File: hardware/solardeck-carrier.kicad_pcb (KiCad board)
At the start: 6 copper layers, 222 x 160 mm, 24 parts, among them J1 DF40C-100DS-0.4V, J2 DF40C-100DS-0.4V, SW1 JS102011SAQN, U1 BQ25895RTWR, U10 W25Q128JVS, U11 DS3231MZ+, U14 TMUX1575PWR, U15 SN74LVC1G08DBVR, U16 VL805-Q6, U18 ST4SIM-200M, U2 TPS62840DLYR, U3 TPS61088RHLR, U4 TPS63020DSJR, U5 BQ25504RGTR, U8 RP2350B, U9 APS6404L-3SQR-SN

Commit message: hardware: fix TMUX1575 fake PN (PWR->YCJR) across all artifacts; make Rule 8 scan comp values
The repo shipped TMUX1575PWR -- a part number that does not exist (TI TMUX1575
is DSBGA-YCJ only, per HARDWARE_SPEC B2/ADR-004). The fake PN was in the netlist
comp value, PCB fp_text, display sheet, BOM/CPL CSVs and both Seeed BOM exports,
while audit Rule 8 only scanned net NAMES, so the ban was silently dead code.

- parse_netlist_comps() added; Rule 8 now audits both nets and comp values
  (negative-tested: a value-embedded TMUX1575PWR is caught).
- All artifacts normalized to TMUX1575YCJR; footprint marked DSBGA-16 with dims
  TBD from TI datasheet (no fabricated package size); display sheet comment
  corrected from the banned '8-Channel' framing to 4-channel x2 devices.

Co-Authored-By: DeepSeek V4-Flash 0731 <noreply@anthropic.com>
Harness: pi (openrouter/deepseek/deepseek-v4-flash-0731, session 01a15a7c)
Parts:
- U14: value TMUX1575PWR -> TMUX1575YCJR; footprint Package_SO:TSSOP-24_4.4x7.8mm_P0.65mm -> DSBGA-16 (dims per TI datasheet; see ADR-004)
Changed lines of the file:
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@@
   )
   ;; Display Section: TMUX1575 (U14), IT8951 40-pin FPC (J_EPDC), Palm Gate (U15)
-  (footprint "Package_SO:TSSOP-24_4.4x7.8mm_P0.65mm" (layer "F.Cu")
+  (footprint "DSBGA-16 (dims per TI datasheet; see ADR-004)" (layer "F.Cu")
     (at 85.0 25.0)
     (fp_text reference "U14" (at 0 -4.5) (layer "F.SilkS") (effects (font (size 1 1) (thickness 0.15))))
-    (fp_text value "TMUX1575PWR" (at 0 4.5) (layer "F.Fab") (effects (font (size 1 1) (thickness 0.15))))
+    (fp_text value "TMUX1575YCJR" (at 0 4.5) (layer "F.Fab") (effects (font (size 1 1) (thickness 0.15))))
     (pad "1" smd rect (at -2.8 -3.575) (size 1.4 0.4) (layers "F.Cu" "F.Paste" "F.Mask"))
   )

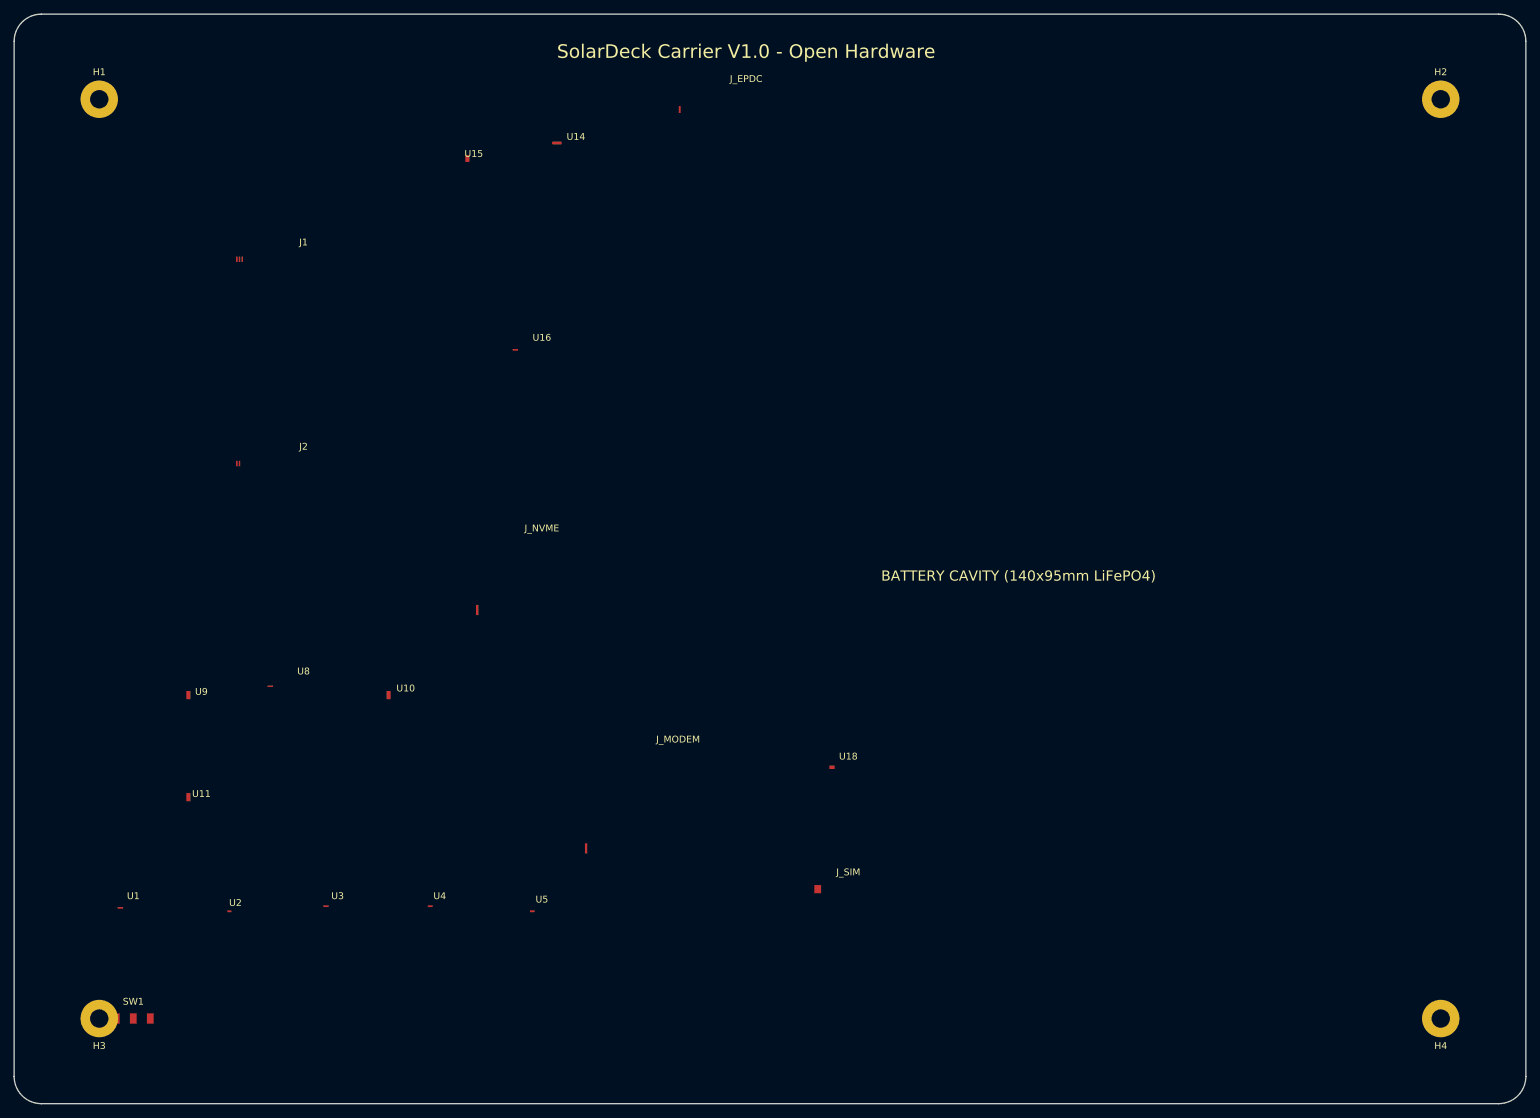
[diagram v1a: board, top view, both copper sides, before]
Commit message: schematic: capture 10 sensor/power/io BOM line items into the schematic layer (20/62 -> 30/62)
Adds U19-U28 with datasheet-anchored footprints and REAL sourced LCSC part
numbers (verified 2026-11-02): TPS22918DBVR, INA3221AIRGVR, BQ27441-G1A,
TPS2051BDBVR (power); BMA400, BMP390, TMP112AIDRLR (compute); TUSB320RWBR,
TXU0104PWR, MAX98357A (io).

Files moved in lockstep: .kicad_sch symbol blocks, netlist comps, BOM CSV rows,
CPL centroids (inside 222x160 board), kicad_pcb fp_text reference labels
(reference-grade single pads per U5/U14 convention; full pad maps and routing
remain the stated 'unrouted PCB' phase).

scripts/capture_schematic_parts.py is the generator + assert (Phase 11 contract:
netlist == BOM == CPL == 30 designators). spec_values schematic_coverage_baseline
20 -> 30; prose in README/BOM/HANDOFF normalized; STATUS.md regenerated.

Co-Authored-By: DeepSeek V4-Flash 0731 <noreply@anthropic.com>
Harness: pi (openrouter/deepseek/deepseek-v4-flash-0731, session 01a15a7c)
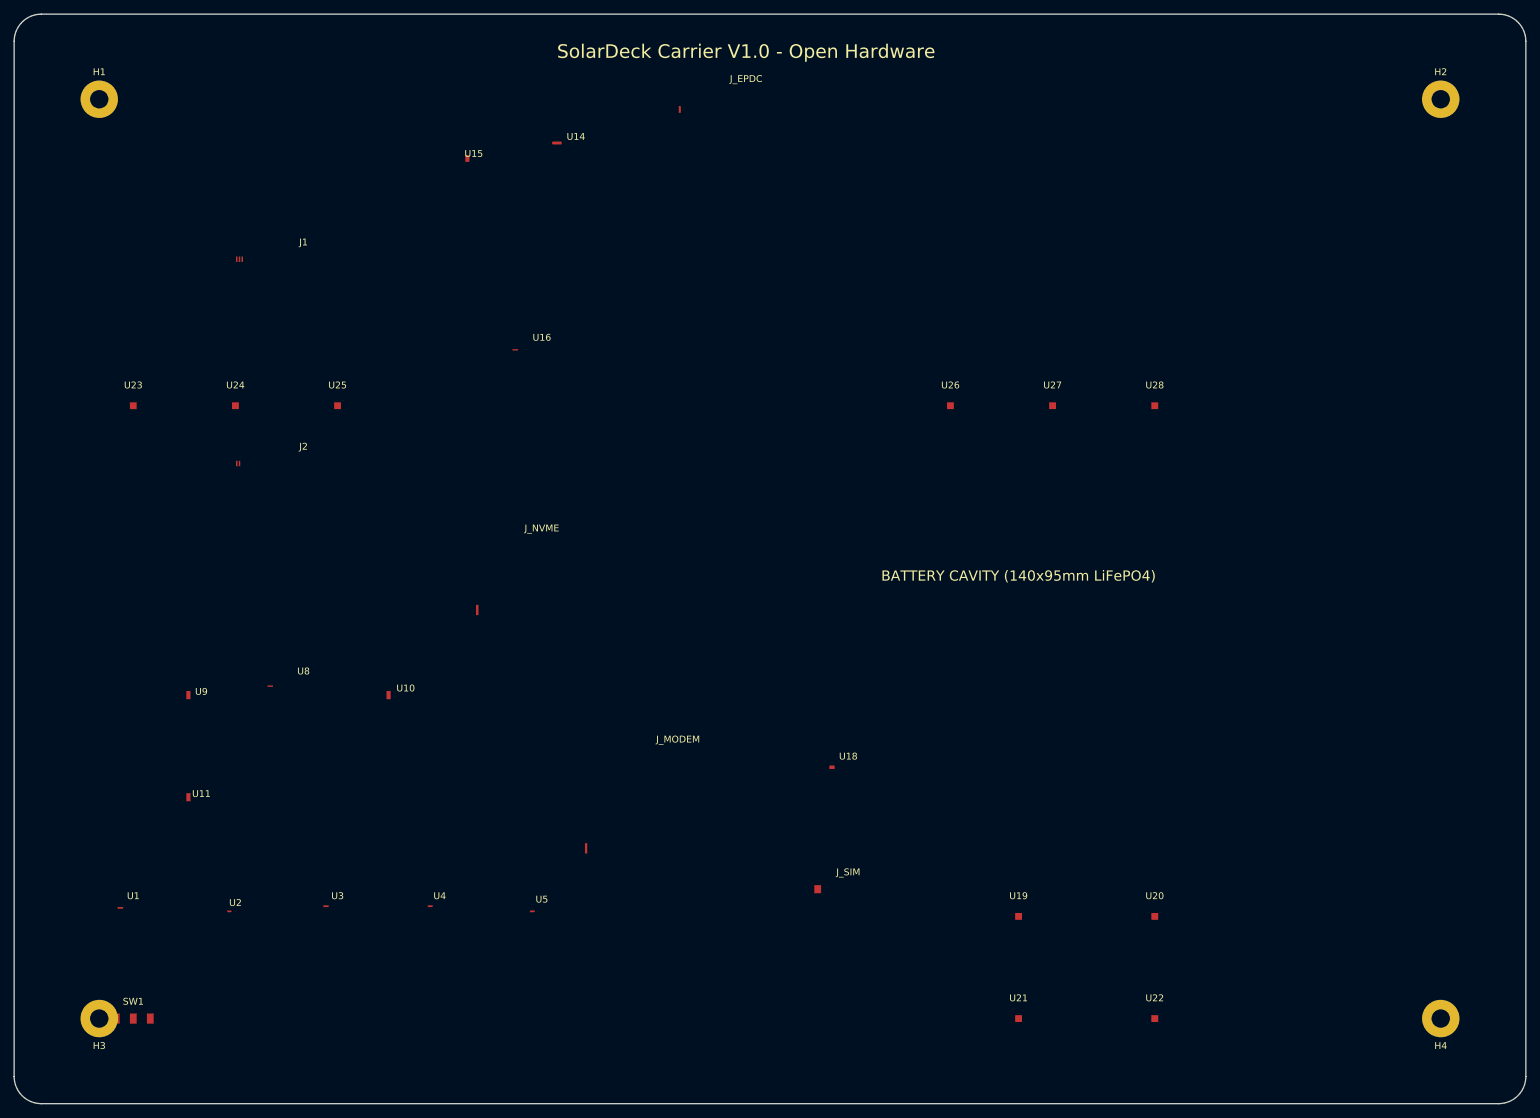
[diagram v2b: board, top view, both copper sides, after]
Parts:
- added U19: TPS22918DBVR, Package_TO_SOT_SMD:SOT-23-6, F.Cu at (150.0, 135.0)
- added U20: INA3221AIRGVR, Package_DFN_QFN:VQFN-16-1EP_4x4mm_P0.65mm, F.Cu at (170.0, 135.0)
- added U21: BQ27441-G1A, Package_DFN_QFN:VSON-12_2.5x4mm_P0.5mm, F.Cu at (150.0, 150.0)
- added U22: TPS2051BDBVR, Package_TO_SOT_SMD:SOT-23-5, F.Cu at (170.0, 150.0)
- added U23: BMA400, Package_LGA:LGA-12_2x2mm_P0.5mm, F.Cu at (20.0, 60.0)
- added U24: BMP390, Package_LGA:LGA-10_2x2mm_P0.5mm, F.Cu at (35.0, 60.0)
- added U25: TMP112AIDRLR, Package_TO_SOT_SMD:SOT-563, F.Cu at (50.0, 60.0)
- added U26: TUSB320RWBR, Package_DFN_QFN:X2QFN-12_1.6x1.6mm_P0.4mm, F.Cu at (140.0, 60.0)
- added U27: TXU0104PWR, Package_SO:TSSOP-14_4.4x5mm_P0.65mm, F.Cu at (155.0, 60.0)
- added U28: MAX98357A, Package_DFN_QFN:WQFN-16-1EP_3x3mm_P0.5mm, F.Cu at (170.0, 60.0)
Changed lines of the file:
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@@
     (pad "1" smd rect (at -4.5 -4.0) (size 1.0 1.2) (layers "F.Cu" "F.Paste" "F.Mask"))
   )
+  (footprint "Package_TO_SOT_SMD:SOT-23-6" (layer "F.Cu")
+    (at 150.0 135.0)
+    (fp_text reference "U19" (at 0 -3.0) (layer "F.SilkS") (effects (font (size 1 1) (thickness 0.15))))
+    (fp_text value "TPS22918DBVR" (at 0 3.0) (layer "F.Fab") (effects (font (size 1 1) (thickness 0.15))))
+    (pad "1" smd rect (at 0 0) (size 1.0 1.0) (layers "F.Cu" "F.Paste" "F.Mask"))
+  )
+  (footprint "Package_DFN_QFN:VQFN-16-1EP_4x4mm_P0.65mm" (layer "F.Cu")
+    (at 170.0 135.0)
+    (fp_text reference "U20" (at 0 -3.0) (layer "F.SilkS") (effects (font (size 1 1) (thickness 0.15))))
+    (fp_text value "INA3221AIRGVR" (at 0 3.0) (layer "F.Fab") (effects (font (size 1 1) (thickness 0.15))))
+    (pad "1" smd rect (at 0 0) (size 1.0 1.0) (layers "F.Cu" "F.Paste" "F.Mask"))
+  )
+  (footprint "Package_DFN_QFN:VSON-12_2.5x4mm_P0.5mm" (layer "F.Cu")
+    (at 150.0 150.0)
+    (fp_text reference "U21" (at 0 -3.0) (layer "F.SilkS") (effects (font (size 1 1) (thickness 0.15))))
+    (fp_text value "BQ27441-G1A" (at 0 3.0) (layer "F.Fab") (effects (font (size 1 1) (thickness 0.15))))
+    (pad "1" smd rect (at 0 0) (size 1.0 1.0) (layers "F.Cu" "F.Paste" "F.Mask"))
+  )
+  (footprint "Package_TO_SOT_SMD:SOT-23-5" (layer "F.Cu")
+    (at 170.0 150.0)
+    (fp_text reference "U22" (at 0 -3.0) (layer "F.SilkS") (effects (font (size 1 1) (thickness 0.15))))
+    (fp_text value "TPS2051BDBVR" (at 0 3.0) (layer "F.Fab") (effects (font (size 1 1) (thickness 0.15))))
+    (pad "1" smd rect (at 0 0) (size 1.0 1.0) (layers "F.Cu" "F.Paste" "F.Mask"))
+  )
+  (footprint "Package_LGA:LGA-12_2x2mm_P0.5mm" (layer "F.Cu")
+    (at 20.0 60.0)
+    (fp_text reference "U23" (at 0 -3.0) (layer "F.SilkS") (effects (font (size 1 1) (thickness 0.15))))
+    (fp_text value "BMA400" (at 0 3.0) (layer "F.Fab") (effects (font (size 1 1) (thickness 0.15))))
+    (pad "1" smd rect (at 0 0) (size 1.0 1.0) (layers "F.Cu" "F.Paste" "F.Mask"))
+  )
+  (footprint "Package_LGA:LGA-10_2x2mm_P0.5mm" (layer "F.Cu")
+    (at 35.0 60.0)
+    (fp_text reference "U24" (at 0 -3.0) (layer "F.SilkS") (effects (font (size 1 1) (thickness 0.15))))
+    (fp_text value "BMP390" (at 0 3.0) (layer "F.Fab") (effects (font (size 1 1) (thickness 0.15))))
+    (pad "1" smd rect (at 0 0) (size 1.0 1.0) (layers "F.Cu" "F.Paste" "F.Mask"))
+  )
+  (footprint "Package_TO_SOT_SMD:SOT-563" (layer "F.Cu")
+    (at 50.0 60.0)
+    (fp_text reference "U25" (at 0 -3.0) (layer "F.SilkS") (effects (font (size 1 1) (thickness 0.15))))
+    (fp_text value "TMP112AIDRLR" (at 0 3.0) (layer "F.Fab") (effects (font (size 1 1) (thickness 0.15))))
+    (pad "1" smd rect (at 0 0) (size 1.0 1.0) (layers "F.Cu" "F.Paste" "F.Mask"))
+  )
+  (footprint "Package_DFN_QFN:X2QFN-12_1.6x1.6mm_P0.4mm" (layer "F.Cu")
+    (at 140.0 60.0)
+    (fp_text reference "U26" (at 0 -3.0) (layer "F.SilkS") (effects (font (size 1 1) (thickness 0.15))))
+    (fp_text value "TUSB320RWBR" (at 0 3.0) (layer "F.Fab") (effects (font (size 1 1) (thickness 0.15))))
+    (pad "1" smd rect (at 0 0) (size 1.0 1.0) (layers "F.Cu" "F.Paste" "F.Mask"))
+  )
+  (footprint "Package_SO:TSSOP-14_4.4x5mm_P0.65mm" (layer "F.Cu")
+    (at 155.0 60.0)
+    (fp_text reference "U27" (at 0 -3.0) (layer "F.SilkS") (effects (font (size 1 1) (thickness 0.15))))
+    (fp_text value "TXU0104PWR" (at 0 3.0) (layer "F.Fab") (effects (font (size 1 1) (thickness 0.15))))
+    (pad "1" smd rect (at 0 0) (size 1.0 1.0) (layers "F.Cu" "F.Paste" "F.Mask"))
+  )
+  (footprint "Package_DFN_QFN:WQFN-16-1EP_3x3mm_P0.5mm" (layer "F.Cu")
+    (at 170.0 60.0)
+    (fp_text reference "U28" (at 0 -3.0) (layer "F.SilkS") (effects (font (size 1 1) (thickness 0.15))))
+    (fp_text value "MAX98357A" (at 0 3.0) (layer "F.Fab") (effects (font (size 1 1) (thickness 0.15))))
+    (pad "1" smd rect (at 0 0) (size 1.0 1.0) (layers "F.Cu" "F.Paste" "F.Mask"))
+  )
 )
